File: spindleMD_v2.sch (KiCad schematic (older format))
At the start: 44 parts, among them J1 Conn_LogicPower, J2 Conn_SWD, J3 Conn_UART, J4 Conn_I2C, J5 Conn_Encoder, J6 Conn_GPIO, J7 Conn_MotorPower, J8 Conn_drivePower, J9 Conn_Motor, SW1 USER_BUTTON, SW2 RESET_BUTTON, U1 L7805, U2 L78L33_SOT89, U3 IK0505SA

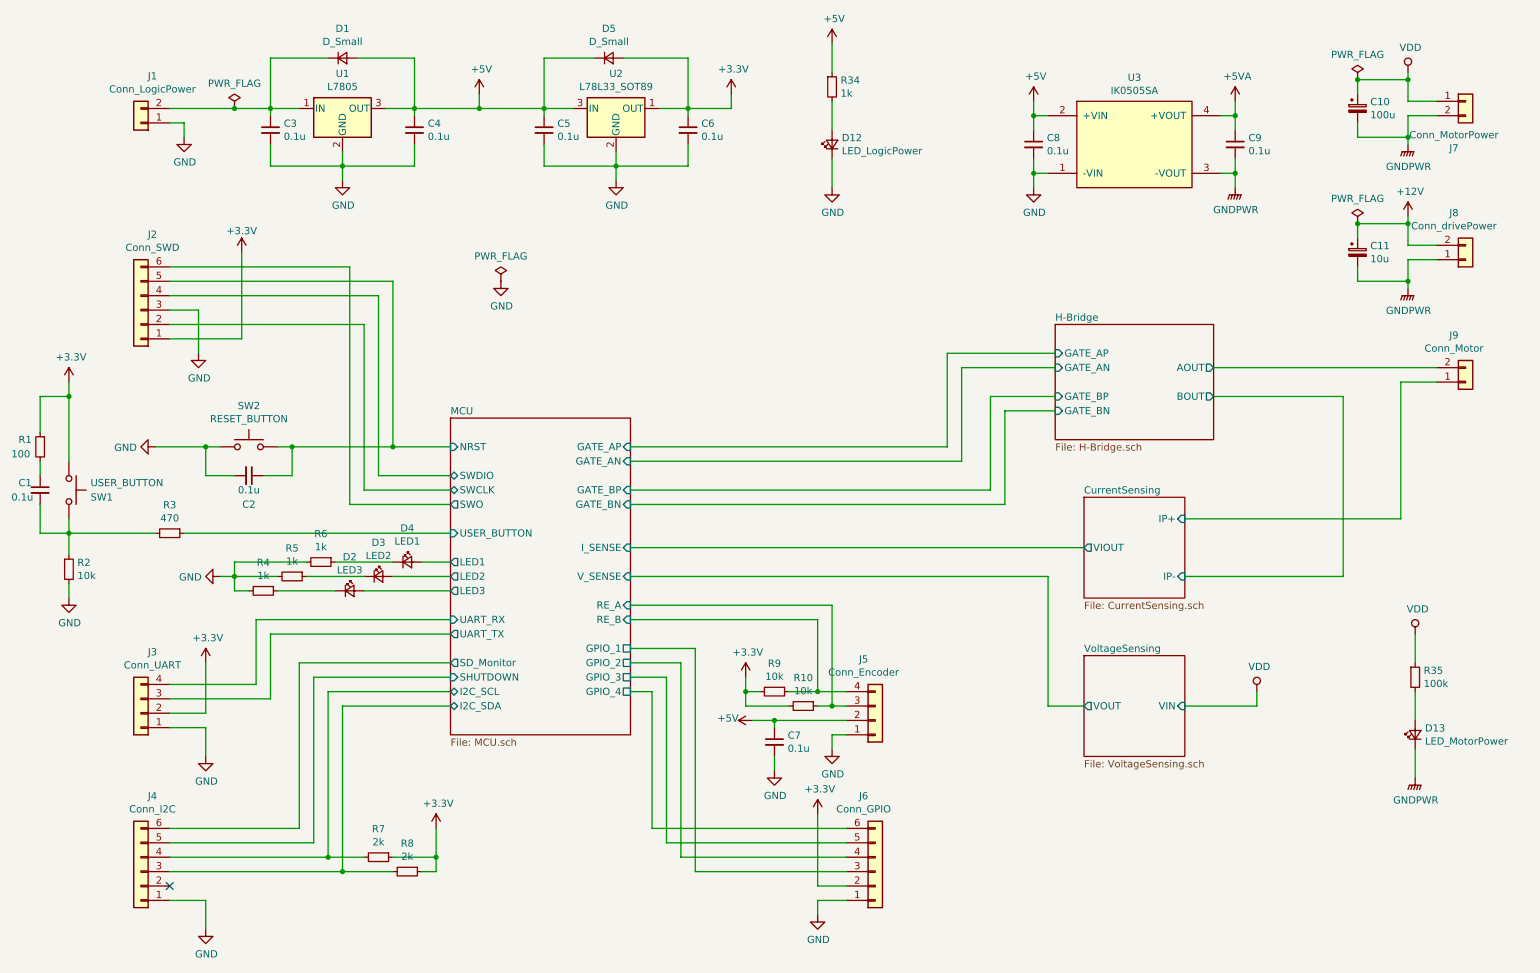
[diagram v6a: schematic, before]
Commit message: 電流センサ電源パスコン追加
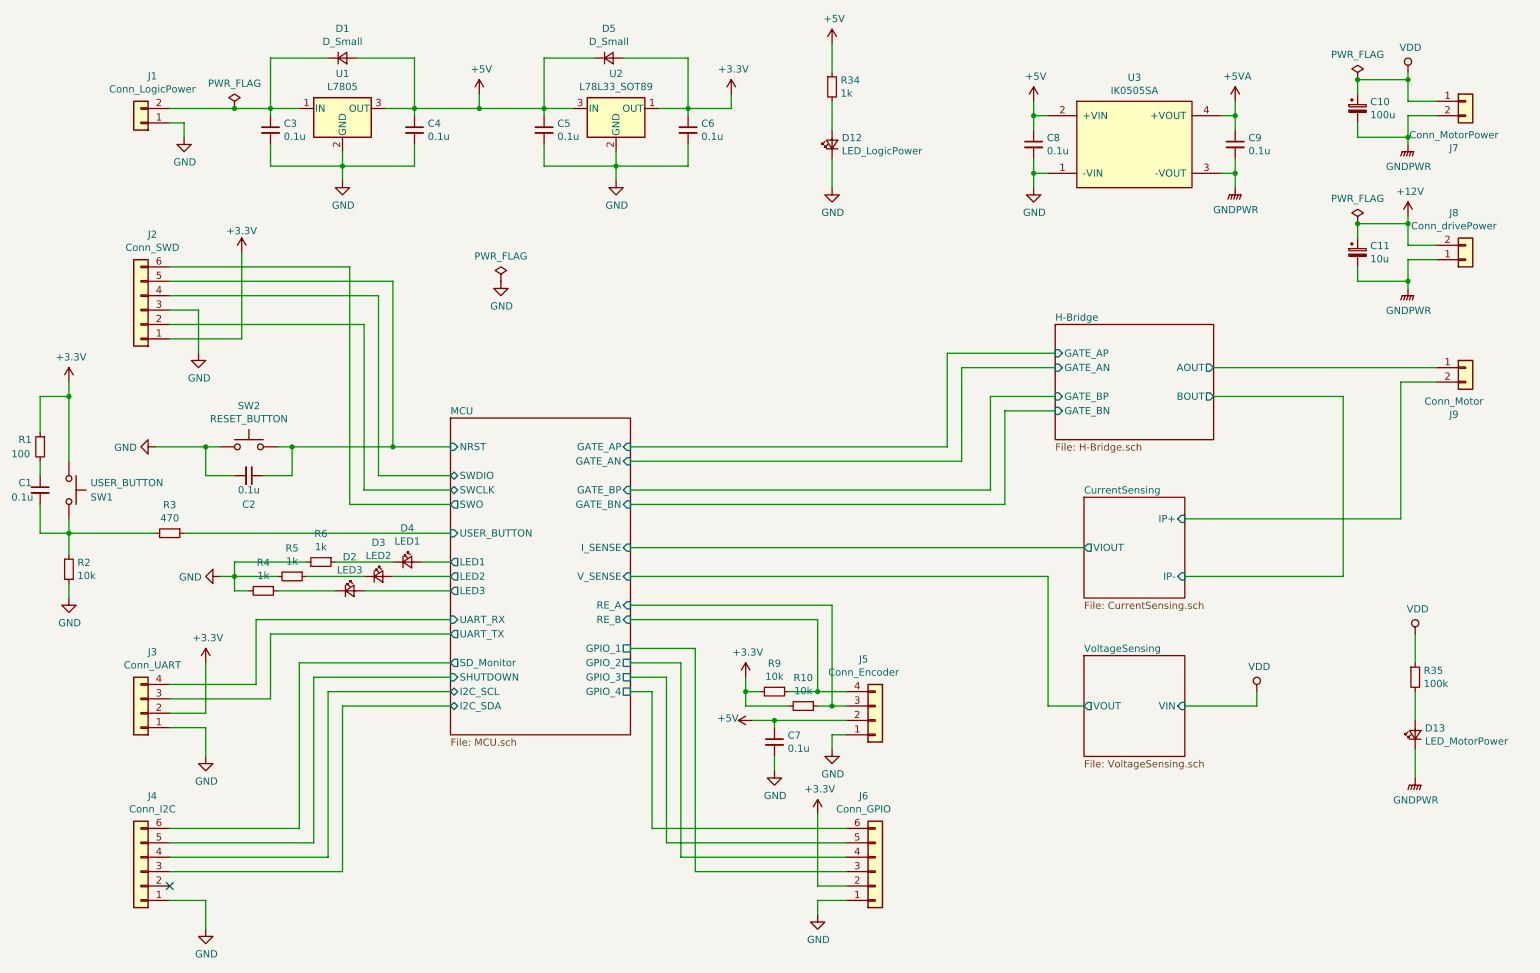
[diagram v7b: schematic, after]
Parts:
- removed R7, R8: 2k, Resistors_SMD:R_0603_HandSoldering, symbol Device:R_Small
- C1, C2, C3, C4, C5, C6, C7, C8, C9: footprint Capacitors_SMD:C_0805_HandSoldering -> Capacitors_SMD:C_0603_HandSoldering
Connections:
- net CurrentSensing/IP+: now also J9.2 (Pin_2); no longer J9.1 (Pin_1)
- net H-Bridge/AOUT: now also J9.1 (Pin_1); no longer J9.2 (Pin_2)
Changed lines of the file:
@@
 F 0 "C9" H 9242 1696 50  0000 L CNN
 F 1 "0.1u" H 9242 1605 50  0000 L CNN
-F 2 "Capacitors_SMD:C_0805_HandSoldering" H 9150 1650 50  0001 C CNN
+F 2 "Capacitors_SMD:C_0603_HandSoldering" H 9150 1650 50  0001 C CNN
 F 3 "~" H 9150 1650 50  0001 C CNN
 	1    9150 1650
@@
 F 0 "C8" H 7842 1696 50  0000 L CNN
 F 1 "0.1u" H 7842 1605 50  0000 L CNN
-F 2 "Capacitors_SMD:C_0805_HandSoldering" H 7750 1650 50  0001 C CNN
+F 2 "Capacitors_SMD:C_0603_HandSoldering" H 7750 1650 50  0001 C CNN
 F 3 "~" H 7750 1650 50  0001 C CNN
 	1    7750 1650
@@
 F 0 "C3" H 2542 1596 50  0000 L CNN
 F 1 "0.1u" H 2542 1505 50  0000 L CNN
-F 2 "Capacitors_SMD:C_0805_HandSoldering" H 2450 1550 50  0001 C CNN
+F 2 "Capacitors_SMD:C_0603_HandSoldering" H 2450 1550 50  0001 C CNN
 F 3 "~" H 2450 1550 50  0001 C CNN
 	1    2450 1550
@@
 F 0 "C4" H 3542 1596 50  0000 L CNN
 F 1 "0.1u" H 3542 1505 50  0000 L CNN
-F 2 "Capacitors_SMD:C_0805_HandSoldering" H 3450 1550 50  0001 C CNN
+F 2 "Capacitors_SMD:C_0603_HandSoldering" H 3450 1550 50  0001 C CNN
 F 3 "~" H 3450 1550 50  0001 C CNN
 	1    3450 1550
@@
 F 0 "C5" H 4442 1596 50  0000 L CNN
 F 1 "0.1u" H 4442 1505 50  0000 L CNN
-F 2 "Capacitors_SMD:C_0805_HandSoldering" H 4350 1550 50  0001 C CNN
+F 2 "Capacitors_SMD:C_0603_HandSoldering" H 4350 1550 50  0001 C CNN
 F 3 "~" H 4350 1550 50  0001 C CNN
 	1    4350 1550
@@
 F 0 "C6" H 5442 1596 50  0000 L CNN
 F 1 "0.1u" H 5442 1505 50  0000 L CNN
-F 2 "Capacitors_SMD:C_0805_HandSoldering" H 5350 1550 50  0001 C CNN
+F 2 "Capacitors_SMD:C_0603_HandSoldering" H 5350 1550 50  0001 C CNN
 F 3 "~" H 5350 1550 50  0001 C CNN
 	1    5350 1550
@@
 L Connector_Generic:Conn_01x02 J9
 U 1 1 5CABACCB
-P 10750 3300
-F 0 "J9" H 10669 2975 50  0000 C CNN
-F 1 "Conn_Motor" H 10669 3066 50  0000 C CNN
-F 2 "Connectors_JST:JST_VH_B2P-VH-B_2x3.96mm_Vertical" H 10750 3300 50  0001 C CNN
-F 3 "~" H 10750 3300 50  0001 C CNN
-	1    10750 3300
-	1    0    0    1
+P 10750 3200
+F 0 "J9" H 10669 2875 50  0000 C CNN
+F 1 "Conn_Motor" H 10669 2966 50  0000 C CNN
+F 2 "Connectors_JST:JST_VH_B2P-VH-B_2x3.96mm_Vertical" H 10750 3200 50  0001 C CNN
+F 3 "~" H 10750 3200 50  0001 C CNN
+	1    10750 3200
+	1    0    0    -1
 $EndComp
 Wire Wire Line
@@
 Wire Wire Line
 	5400 6700 6450 6700
-$Comp
-L Device:R_Small R8
-U 1 1 5CC09AB0
-P 3400 6700
-F 0 "R8" V 3204 6700 50  0000 C CNN
-F 1 "2k" V 3295 6700 50  0000 C CNN
-F 2 "Resistors_SMD:R_0603_HandSoldering" H 3400 6700 50  0001 C CNN
-F 3 "~" H 3400 6700 50  0001 C CNN
-	1    3400 6700
-	0    1    1    0
-$EndComp
-$Comp
-L Device:R_Small R7
-U 1 1 5CC09CE3
-P 3200 6600
-F 0 "R7" V 3004 6600 50  0000 C CNN
-F 1 "2k" V 3095 6600 50  0000 C CNN
-F 2 "Resistors_SMD:R_0603_HandSoldering" H 3200 6600 50  0001 C CNN
-F 3 "~" H 3200 6600 50  0001 C CNN
-	1    3200 6600
-	0    1    1    0
-$EndComp
-Wire Wire Line
-	2850 6600 3100 6600
-Connection ~ 2850 6600
-Wire Wire Line
-	3300 6700 2950 6700
-Connection ~ 2950 6700
-Wire Wire Line
-	3300 6600 3600 6600
-Wire Wire Line
-	3600 6600 3600 6700
-Wire Wire Line
-	3600 6700 3500 6700
-$Comp
-L power:+3.3V #PWR?
-U 1 1 5CC35E3C
-P 3600 6400
-AR Path="/5C77D603/5CC35E3C" Ref="#PWR?"  Part="1"
-AR Path="/5CC35E3C" Ref="#PWR012"  Part="1"
-F 0 "#PWR012" H 3600 6250 50  0001 C CNN
-F 1 "+3.3V" H 3615 6573 50  0000 C CNN
-F 2 "" H 3600 6400 50  0001 C CNN
-F 3 "" H 3600 6400 50  0001 C CNN
-	1    3600 6400
-	1    0    0    -1
-$EndComp
-Wire Wire Line
-	3600 6400 3600 6600
-Connection ~ 3600 6600
 $Comp
 L power:+5V #PWR?
@@
 F 0 "C7" H 6042 5846 50  0000 L CNN
 F 1 "0.1u" H 6042 5755 50  0000 L CNN
-F 2 "Capacitors_SMD:C_0805_HandSoldering" H 5950 5800 50  0001 C CNN
+F 2 "Capacitors_SMD:C_0603_HandSoldering" H 5950 5800 50  0001 C CNN
 F 3 "~" H 5950 5800 50  0001 C CNN
 	1    5950 5800
@@
 F 0 "C2" V 2500 3950 50  0000 C CNN
 F 1 "0.1u" V 2400 3950 50  0000 C CNN
-F 2 "Capacitors_SMD:C_0805_HandSoldering" H 2300 3950 50  0001 C CNN
+F 2 "Capacitors_SMD:C_0603_HandSoldering" H 2300 3950 50  0001 C CNN
 F 3 "~" H 2300 3950 50  0001 C CNN
 	1    2300 3950
@@
 F 0 "C1" H 700 4100 50  0000 L CNN
 F 1 "0.1u" H 650 4000 50  0000 L CNN
-F 2 "Capacitors_SMD:C_0805_HandSoldering" H 850 4050 50  0001 C CNN
+F 2 "Capacitors_SMD:C_0603_HandSoldering" H 850 4050 50  0001 C CNN
 F 3 "~" H 850 4050 50  0001 C CNN
 	1    850  4050

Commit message: kicadバージョン更新
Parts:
- U3: symbol mylib:IK0505SA -> spindleMD_v2-rescue:IK0505SA-mylib
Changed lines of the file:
@@
 EESchema Schematic File Version 4
 LIBS:spindleMD_v2-cache
-EELAYER 26 0
+EELAYER 29 0
 EELAYER END
 $Descr A4 11693 8268
@@
 $EndComp
 $Comp
-L mylib:IK0505SA U3
+L spindleMD_v2-rescue:IK0505SA-mylib U3
 U 1 1 5C7D2B90
 P 8450 1650
